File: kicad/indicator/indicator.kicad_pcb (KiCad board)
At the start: 2 copper layers, 30.7 x 11.7 mm, 9 parts, among them J1 Conn_01x03, Q1 2N3904, Q2 2N3904

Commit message: update a PCB a bit
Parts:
- moved J1 0.51 mm to (21.6, 21.5)
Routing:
- net VCC: track 4.58 -> 4.07 mm
- net Net-(J1-Pad3): track 4.61 -> 4.11 mm

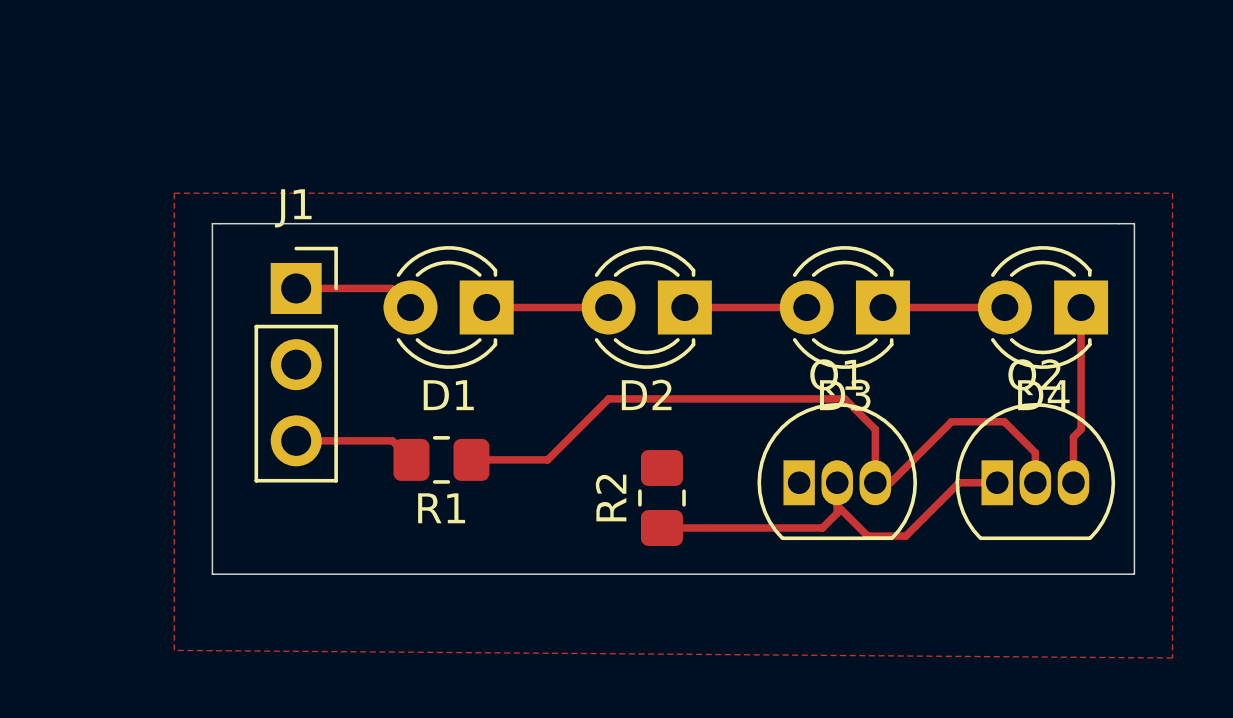
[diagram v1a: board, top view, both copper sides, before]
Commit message: exclude pcb edge disabled.
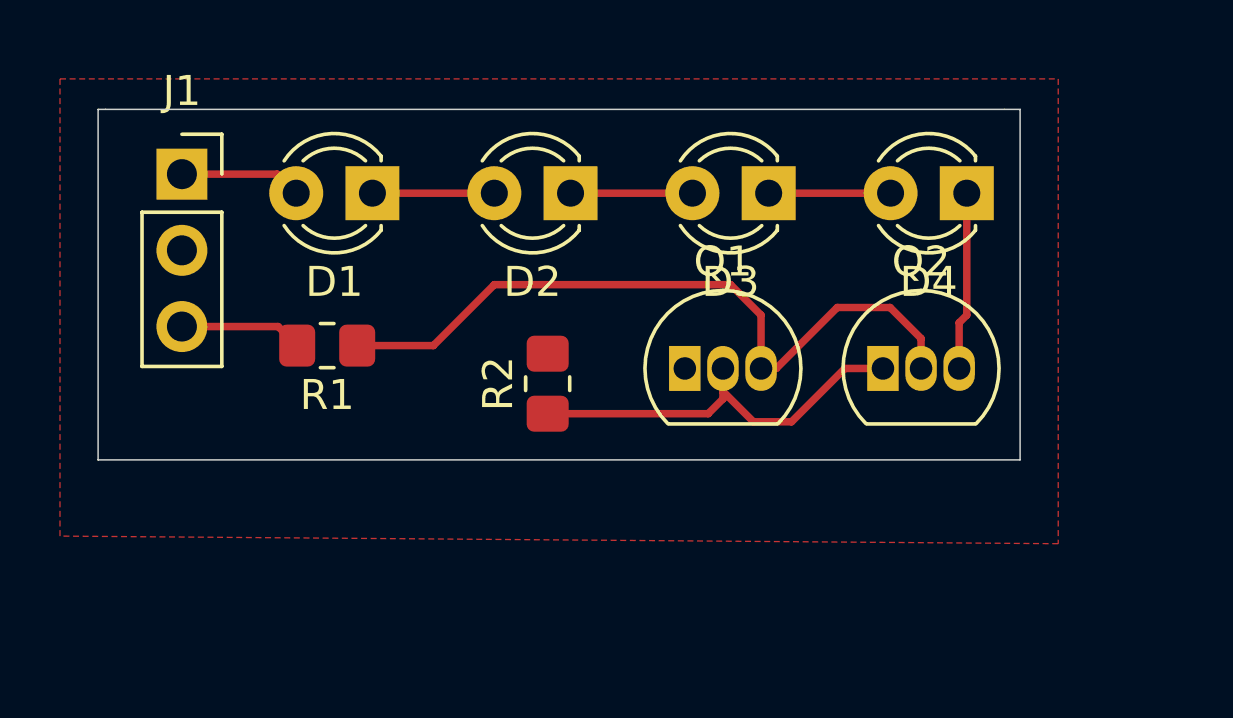
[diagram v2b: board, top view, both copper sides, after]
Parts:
- moved Q1 5.39 mm to (34.5, 24.1)
- moved D1 5.39 mm to (24.1, 18.3)
- moved D3 5.39 mm to (37.3, 18.3)
- moved D4 5.39 mm to (43.9, 18.3)
- moved J1 5.39 mm to (17.8, 17.7)
- moved R1 5.39 mm to (22.6, 23.4)
- moved Q2 5.39 mm to (41.1, 24.1)
- moved D2 5.39 mm to (30.7, 18.3)
- moved R2 5.39 mm to (30.0, 24.6)
